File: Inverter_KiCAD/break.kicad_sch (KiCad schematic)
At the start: 13 parts, among them J8 Conn_01x02, Q9 BUK9637-100E, U21 TC1412, U22 ACPL-077L

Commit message: start schematic Nucleo board
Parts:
- C57, C58, C59, C60: footprint (none) -> Capacitor_SMD:C_0402_1005Metric_Pad0.74x0.62mm_HandSolder
- R30, R31: footprint (none) -> Resistor_SMD:R_0603_1608Metric_Pad0.98x0.95mm_HandSolder
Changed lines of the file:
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@@
       (effects (font (size 1.27 1.27)) (justify left))
     )
-    (property "Footprint" "" (at 100.33 54.61 0)
+    (property "Footprint" "Capacitor_SMD:C_0402_1005Metric_Pad0.74x0.62mm_HandSolder" (at 100.33 54.61 0)
       (effects (font (size 1.27 1.27)) hide)
     )
@@
       (effects (font (size 1.27 1.27)) (justify left))
     )
-    (property "Footprint" "" (at 53.34 54.61 0)
+    (property "Footprint" "Capacitor_SMD:C_0402_1005Metric_Pad0.74x0.62mm_HandSolder" (at 53.34 54.61 0)
       (effects (font (size 1.27 1.27)) hide)
     )
@@
       (effects (font (size 1.27 1.27)) (justify left))
     )
-    (property "Footprint" "" (at 88.9 31.75 0)
+    (property "Footprint" "Resistor_SMD:R_0603_1608Metric_Pad0.98x0.95mm_HandSolder" (at 88.9 31.75 0)
       (effects (font (size 1.27 1.27)) hide)
     )
@@
       (effects (font (size 1.27 1.27)) (justify left))
     )
-    (property "Footprint" "" (at 109.22 54.61 0)
+    (property "Footprint" "Capacitor_SMD:C_0402_1005Metric_Pad0.74x0.62mm_HandSolder" (at 109.22 54.61 0)
       (effects (font (size 1.27 1.27)) hide)
     )
@@
       (effects (font (size 1.27 1.27)))
     )
-    (property "Footprint" "" (at 36.83 49.53 0)
+    (property "Footprint" "Resistor_SMD:R_0603_1608Metric_Pad0.98x0.95mm_HandSolder" (at 36.83 49.53 0)
       (effects (font (size 1.27 1.27)) hide)
     )
@@
       (effects (font (size 1.27 1.27)) (justify left))
     )
-    (property "Footprint" "" (at 62.23 54.61 0)
-      (effects (font (size 1.27 1.27)) hide)
-    )
+    (property "Footprint" "Capacitor_SMD:C_0402_1005Metric_Pad0.74x0.62mm_HandSolder" (at 62.23 54.61 0)
+      (effects (font (size 1.27 1.27)) hide)
+    )

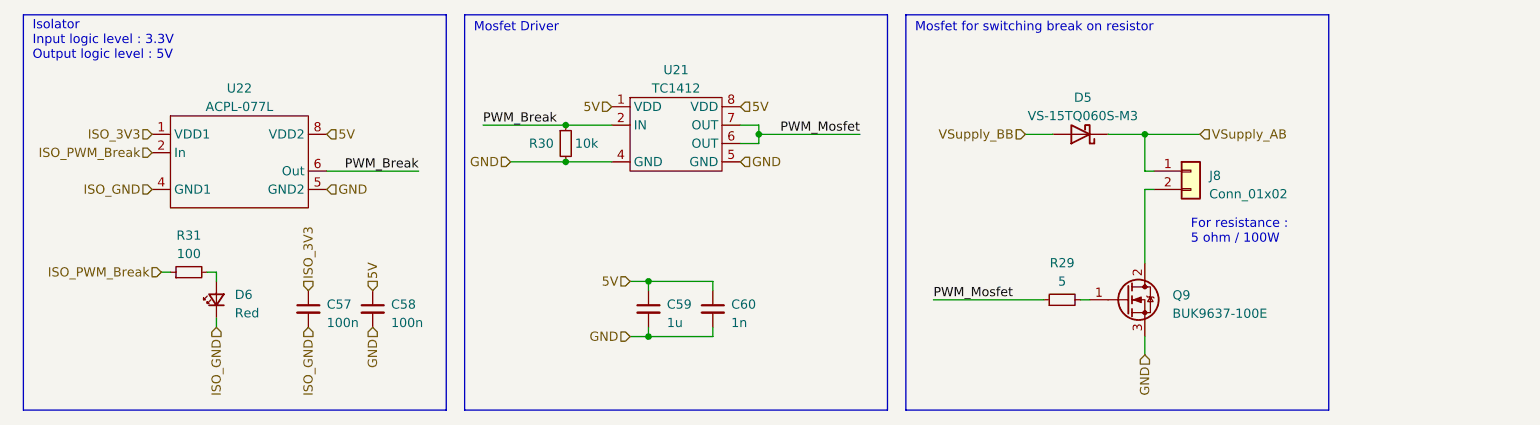
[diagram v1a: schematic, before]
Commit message: clear schematic errors
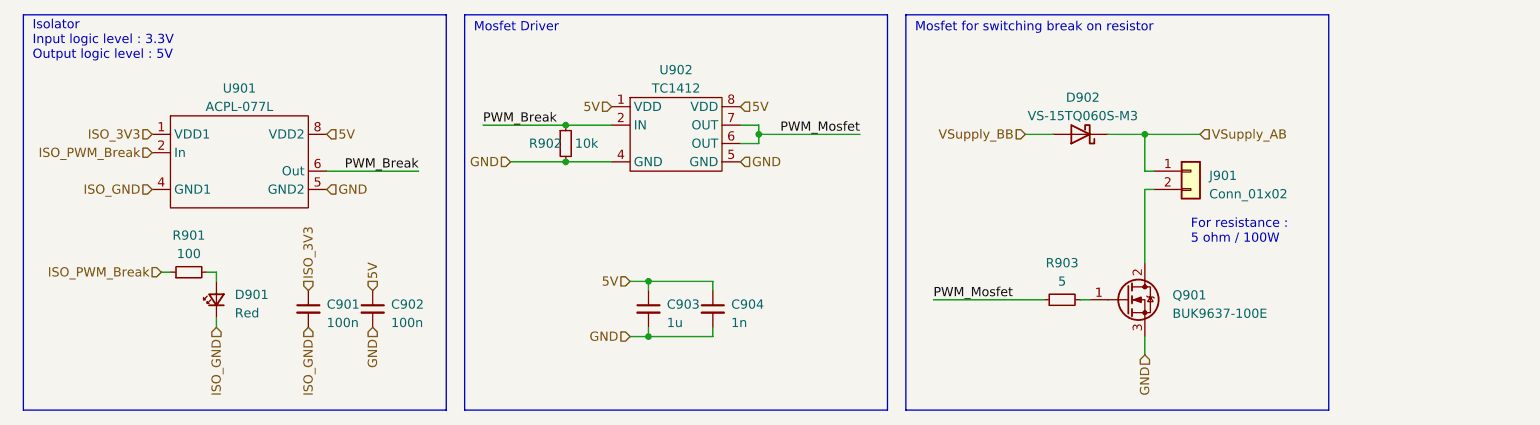
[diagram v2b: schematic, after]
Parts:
- renumbered C57 to C901, C58 to C902, C59 to C903, C60 to C904, D6 to D901, D5 to D902, J8 to J901, Q9 to Q901, R31 to R901, R30 to R902, R29 to R903, U22 to U901, U21 to U902
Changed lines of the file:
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@@
   (symbol (lib_id "Custom:TC1412") (at 104.14 30.48 0) (unit 1)
     (in_bom yes) (on_board yes) (dnp no) (fields_autoplaced)
-    (property "Reference" "U21" (at 104.14 21.59 0)
+    (property "Reference" "U902" (at 104.14 21.59 0)
       (effects (font (size 1.27 1.27)))
     )
@@
       (project "Inverter_KiCAD"
         (path "/5e6c1e3f-0815-454a-8acb-8e3e2d064875/63722f1b-78db-4d3b-ade4-7dd7cc6c956f"
-          (reference "U21") (unit 1)
+          (reference "U902") (unit 1)
         )
       )
@@
   (symbol (lib_id "Device:R_Small") (at 157.48 53.34 90) (unit 1)
     (in_bom yes) (on_board yes) (dnp no) (fields_autoplaced)
-    (property "Reference" "R29" (at 157.48 48.26 90)
+    (property "Reference" "R903" (at 157.48 48.26 90)
       (effects (font (size 1.27 1.27)))
     )
@@
       (project "Inverter_KiCAD"
         (path "/5e6c1e3f-0815-454a-8acb-8e3e2d064875/63722f1b-78db-4d3b-ade4-7dd7cc6c956f"
-          (reference "R29") (unit 1)
+          (reference "R903") (unit 1)
         )
       )
@@
   (symbol (lib_id "Device:C_Small") (at 100.33 54.61 0) (unit 1)
     (in_bom yes) (on_board yes) (dnp no) (fields_autoplaced)
-    (property "Reference" "C59" (at 102.87 53.9813 0)
+    (property "Reference" "C903" (at 102.87 53.9813 0)
       (effects (font (size 1.27 1.27)) (justify left))
     )
@@
       (project "Inverter_KiCAD"
         (path "/5e6c1e3f-0815-454a-8acb-8e3e2d064875/63722f1b-78db-4d3b-ade4-7dd7cc6c956f"
-          (reference "C59") (unit 1)
+          (reference "C903") (unit 1)
         )
       )
@@
   (symbol (lib_id "Device:C_Small") (at 53.34 54.61 0) (unit 1)
     (in_bom yes) (on_board yes) (dnp no) (fields_autoplaced)
-    (property "Reference" "C57" (at 55.88 53.9813 0)
+    (property "Reference" "C901" (at 55.88 53.9813 0)
       (effects (font (size 1.27 1.27)) (justify left))
     )
@@
       (project "Inverter_KiCAD"
         (path "/5e6c1e3f-0815-454a-8acb-8e3e2d064875/63722f1b-78db-4d3b-ade4-7dd7cc6c956f"
-          (reference "C57") (unit 1)
+          (reference "C901") (unit 1)
         )
       )
@@
   (symbol (lib_id "Device:D_Schottky") (at 160.02 30.48 180) (unit 1)
     (in_bom yes) (on_board yes) (dnp no) (fields_autoplaced)
-    (property "Reference" "D5" (at 160.3375 25.4 0)
+    (property "Reference" "D902" (at 160.3375 25.4 0)
       (effects (font (size 1.27 1.27)))
     )
@@
       (project "Inverter_KiCAD"
         (path "/5e6c1e3f-0815-454a-8acb-8e3e2d064875/63722f1b-78db-4d3b-ade4-7dd7cc6c956f"
-          (reference "D5") (unit 1)
+          (reference "D902") (unit 1)
         )
       )
@@
   (symbol (lib_id "Connector_Generic:Conn_01x02") (at 175.26 35.56 0) (unit 1)
     (in_bom yes) (on_board yes) (dnp no) (fields_autoplaced)
-    (property "Reference" "J8" (at 177.8 36.195 0)
+    (property "Reference" "J901" (at 177.8 36.195 0)
       (effects (font (size 1.27 1.27)) (justify left))
     )
@@
       (project "Inverter_KiCAD"
         (path "/5e6c1e3f-0815-454a-8acb-8e3e2d064875/63722f1b-78db-4d3b-ade4-7dd7cc6c956f"
-          (reference "J8") (unit 1)
+          (reference "J901") (unit 1)
         )
       )
@@
   (symbol (lib_id "Device:LED_Small") (at 40.64 53.34 90) (unit 1)
     (in_bom yes) (on_board yes) (dnp no) (fields_autoplaced)
-    (property "Reference" "D6" (at 43.18 52.6415 90)
+    (property "Reference" "D901" (at 43.18 52.6415 90)
       (effects (font (size 1.27 1.27)) (justify right))
     )
@@
       (project "Inverter_KiCAD"
         (path "/5e6c1e3f-0815-454a-8acb-8e3e2d064875/63722f1b-78db-4d3b-ade4-7dd7cc6c956f"
-          (reference "D6") (unit 1)
+          (reference "D901") (unit 1)
         )
       )
@@
   (symbol (lib_id "Device:R_Small") (at 88.9 31.75 0) (unit 1)
     (in_bom yes) (on_board yes) (dnp no)
-    (property "Reference" "R30" (at 83.82 31.75 0)
+    (property "Reference" "R902" (at 83.82 31.75 0)
       (effects (font (size 1.27 1.27)) (justify left))
     )
@@
       (project "Inverter_KiCAD"
         (path "/5e6c1e3f-0815-454a-8acb-8e3e2d064875/63722f1b-78db-4d3b-ade4-7dd7cc6c956f"
-          (reference "R30") (unit 1)
+          (reference "R902") (unit 1)
         )
       )
@@
   (symbol (lib_id "Custom:ACPL-077L") (at 44.45 34.29 0) (unit 1)
     (in_bom yes) (on_board yes) (dnp no) (fields_autoplaced)
-    (property "Reference" "U22" (at 43.815 24.13 0)
+    (property "Reference" "U901" (at 43.815 24.13 0)
       (effects (font (size 1.27 1.27)))
     )
@@
       (project "Inverter_KiCAD"
         (path "/5e6c1e3f-0815-454a-8acb-8e3e2d064875/63722f1b-78db-4d3b-ade4-7dd7cc6c956f"
-          (reference "U22") (unit 1)
+          (reference "U901") (unit 1)
         )
       )
@@
   (symbol (lib_id "Transistor_FET:IRFS4229") (at 166.37 53.34 0) (unit 1)
     (in_bom yes) (on_board yes) (dnp no) (fields_autoplaced)
-    (property "Reference" "Q9" (at 172.72 52.705 0)
+    (property "Reference" "Q901" (at 172.72 52.705 0)
       (effects (font (size 1.27 1.27)) (justify left))
     )
@@
       (project "Inverter_KiCAD"
         (path "/5e6c1e3f-0815-454a-8acb-8e3e2d064875/63722f1b-78db-4d3b-ade4-7dd7cc6c956f"
-          (reference "Q9") (unit 1)
+          (reference "Q901") (unit 1)
         )
       )
@@
   (symbol (lib_id "Device:C_Small") (at 109.22 54.61 0) (unit 1)
     (in_bom yes) (on_board yes) (dnp no) (fields_autoplaced)
-    (property "Reference" "C60" (at 111.76 53.9813 0)
+    (property "Reference" "C904" (at 111.76 53.9813 0)
       (effects (font (size 1.27 1.27)) (justify left))
     )
@@
       (project "Inverter_KiCAD"
         (path "/5e6c1e3f-0815-454a-8acb-8e3e2d064875/63722f1b-78db-4d3b-ade4-7dd7cc6c956f"
-          (reference "C60") (unit 1)
+          (reference "C904") (unit 1)
         )
       )
@@
   (symbol (lib_id "Device:R_Small") (at 36.83 49.53 90) (unit 1)
     (in_bom yes) (on_board yes) (dnp no) (fields_autoplaced)
-    (property "Reference" "R31" (at 36.83 44.45 90)
+    (property "Reference" "R901" (at 36.83 44.45 90)
       (effects (font (size 1.27 1.27)))
     )
@@
       (project "Inverter_KiCAD"
         (path "/5e6c1e3f-0815-454a-8acb-8e3e2d064875/63722f1b-78db-4d3b-ade4-7dd7cc6c956f"
-          (reference "R31") (unit 1)
+          (reference "R901") (unit 1)
         )
       )
@@
   (symbol (lib_id "Device:C_Small") (at 62.23 54.61 0) (unit 1)
     (in_bom yes) (on_board yes) (dnp no) (fields_autoplaced)
-    (property "Reference" "C58" (at 64.77 53.9813 0)
+    (property "Reference" "C902" (at 64.77 53.9813 0)
       (effects (font (size 1.27 1.27)) (justify left))
     )
@@
       (project "Inverter_KiCAD"
         (path "/5e6c1e3f-0815-454a-8acb-8e3e2d064875/63722f1b-78db-4d3b-ade4-7dd7cc6c956f"
-          (reference "C58") (unit 1)
-        )
-      )
+          (reference "C902") (unit 1)
+        )
+      )

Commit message: end of sch, start pcb
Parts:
- D901: footprint (none) -> LED_SMD:LED_0603_1608Metric_Pad1.05x0.95mm_HandSolder
- D902: footprint (none) -> Package_TO_SOT_SMD:TO-263-2
- J901: MFR (none) -> 691311700002
- R901, R902: footprint Resistor_SMD:R_0603_1608Metric_Pad0.98x0.95mm_HandSolder -> Resistor_SMD:R_0402_1005Metric_Pad0.72x0.64mm_HandSolder
- U902: footprint (none) -> Package_SO:SOIC-8_3.9x4.9mm_P1.27mm
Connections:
- net VSupply_AB: now also D902.2 (K); no longer D902.1 (K)
- net VSupply_BB: now also D902.3 (A); no longer D902.2 (A)
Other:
- company: (none) -> ENSEA
- title: (none) -> AAP Inverter
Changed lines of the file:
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@@
 (kicad_sch (version 20230121) (generator eeschema)
   (paper "A4")
+  (title_block
+    (title "AAP Inverter")
+    (date "2023-05-01")
+    (company "ENSEA")
+  )
   (junction (at 115.57 30.48) (diameter 0) (color 0 0 0 0)
   )
@@
       (effects (font (size 1.27 1.27)))
     )
-    (property "Footprint" "" (at 99.06 26.67 0)
+    (property "Footprint" "Package_SO:SOIC-8_3.9x4.9mm_P1.27mm" (at 99.06 26.67 0)
       (effects (font (size 1.27 1.27)) hide)
     )
@@
       (effects (font (size 1.27 1.27)))
     )
-    (property "Footprint" "" (at 160.02 30.48 0)
+    (property "Footprint" "Package_TO_SOT_SMD:TO-263-2" (at 160.02 30.48 0)
       (effects (font (size 1.27 1.27)) hide)
     )
@@
       (effects (font (size 1.27 1.27)) hide)
     )
-    (pin "1")
-    (pin "2")
+    (pin "2")
+    (pin "3")
     (instances
       (project "Inverter_KiCAD"
@@
       (effects (font (size 1.27 1.27)) hide)
     )
-    (property "Datasheet" "~" (at 175.26 35.56 0)
+    (property "Datasheet" "https://www.we-online.com/components/products/datasheet/691311700002.pdf" (at 175.26 35.56 0)
+      (effects (font (size 1.27 1.27)) hide)
+    )
+    (property "MFR" "691311700002" (at 175.26 35.56 0)
+      (effects (font (size 1.27 1.27)) hide)
+    )
+    (property "Field5" "" (at 175.26 35.56 0)
       (effects (font (size 1.27 1.27)) hide)
     )
@@
       (effects (font (size 1.27 1.27)) (justify right))
     )
-    (property "Footprint" "" (at 40.64 53.34 90)
+    (property "Footprint" "LED_SMD:LED_0603_1608Metric_Pad1.05x0.95mm_HandSolder" (at 40.64 53.34 90)
       (effects (font (size 1.27 1.27)) hide)
     )
@@
       (effects (font (size 1.27 1.27)) (justify left))
     )
-    (property "Footprint" "Resistor_SMD:R_0603_1608Metric_Pad0.98x0.95mm_HandSolder" (at 88.9 31.75 0)
+    (property "Footprint" "Resistor_SMD:R_0402_1005Metric_Pad0.72x0.64mm_HandSolder" (at 88.9 31.75 0)
       (effects (font (size 1.27 1.27)) hide)
     )
@@
       (effects (font (size 1.27 1.27)))
     )
-    (property "Footprint" "Resistor_SMD:R_0603_1608Metric_Pad0.98x0.95mm_HandSolder" (at 36.83 49.53 0)
-      (effects (font (size 1.27 1.27)) hide)
-    )
+    (property "Footprint" "Resistor_SMD:R_0402_1005Metric_Pad0.72x0.64mm_HandSolder" (at 36.83 49.53 0)
+      (effects (font (size 1.27 1.27)) hide)
+    )

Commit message: rooting done
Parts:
- J901: footprint (none) -> Custom:691311700002
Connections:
- net VSupply_AB: now also J901.2 (Pin_2); no longer J901.1 (Pin_1)
- net Break_Drain_Mosfet: now reaches Q901.2 (D)
- net Break_Drain_Mosfet: now also J901.1 (Pin_1); no longer J901.2 (Pin_2)
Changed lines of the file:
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@@
+    (effects (font (size 1.27 1.27)) (justify right bottom))
+  )
+  (label "Break_Drain_Mosfet" (at 168.91 44.45 180) (fields_autoplaced)
     (effects (font (size 1.27 1.27)) (justify right bottom))
   )
@@
     )
   )
-  (symbol (lib_id "Connector_Generic:Conn_01x02") (at 175.26 35.56 0) (unit 1)
-    (in_bom yes) (on_board yes) (dnp no) (fields_autoplaced)
-    (property "Reference" "J901" (at 177.8 36.195 0)
-      (effects (font (size 1.27 1.27)) (justify left))
-    )
-    (property "Value" "Conn_01x02" (at 177.8 38.735 0)
-      (effects (font (size 1.27 1.27)) (justify left))
-    )
-    (property "Footprint" "" (at 175.26 35.56 0)
-      (effects (font (size 1.27 1.27)) hide)
-    )
-    (property "Datasheet" "https://www.we-online.com/components/products/datasheet/691311700002.pdf" (at 175.26 35.56 0)
-      (effects (font (size 1.27 1.27)) hide)
-    )
-    (property "MFR" "691311700002" (at 175.26 35.56 0)
-      (effects (font (size 1.27 1.27)) hide)
-    )
-    (property "Field5" "" (at 175.26 35.56 0)
-      (effects (font (size 1.27 1.27)) hide)
-    )
+  (symbol (lib_id "Connector_Generic:Conn_01x02") (at 175.26 38.1 0) (mirror x) (unit 1)
+    (in_bom yes) (on_board yes) (dnp no)
+    (property "Reference" "J901" (at 175.26 30.48 0)
+      (effects (font (size 1.27 1.27)))
+    )
+    (property "Value" "Conn_01x02" (at 175.26 33.02 0)
+      (effects (font (size 1.27 1.27)))
+    )
+    (property "Footprint" "Custom:691311700002" (at 175.26 38.1 0)
+      (effects (font (size 1.27 1.27)) hide)
+    )
+    (property "Datasheet" "https://www.we-online.com/components/products/datasheet/691311700002.pdf" (at 175.26 38.1 0)
+      (effects (font (size 1.27 1.27)) hide)
+    )
+    (property "MFR" "691311700002" (at 175.26 38.1 0)
+      (effects (font (size 1.27 1.27)) hide)
+    )
+    (property "Field5" "" (at 175.26 38.1 0)
+      (effects (font (size 1.27 1.27)) hide)
+    )

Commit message: apply changes
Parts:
- added D1: VS-15TQ060S-M3, Package_TO_SOT_SMD:TO-263-2, symbol Device:D_Schottky
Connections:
- net Break_Drain_Mosfet: now also D1.3 (A)
- net VSupply_AB: now also D1.2 (K)
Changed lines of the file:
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@@
   (junction (at 115.57 30.48) (diameter 0) (color 0 0 0 0)
   )
+  (junction (at 168.91 33.02) (diameter 0) (color 0 0 0 0)
+  )
+  (junction (at 168.91 40.64) (diameter 0) (color 0 0 0 0)
+  )
   (junction (at 88.9 29.21) (diameter 0) (color 0 0 0 0)
   )
@@
     (stroke (width 0) (type default))
   )
-  (wire (pts (xy 168.91 38.1) (xy 168.91 48.26))
+  (wire (pts (xy 168.91 38.1) (xy 168.91 40.64))
     (stroke (width 0) (type default))
   )
@@
     (stroke (width 0) (type default))
   )
+  (wire (pts (xy 165.1 33.02) (xy 168.91 33.02))
+    (stroke (width 0) (type default))
+  )
   (wire (pts (xy 115.57 30.48) (xy 115.57 31.75))
     (stroke (width 0) (type default))
   )
+  (wire (pts (xy 168.91 40.64) (xy 168.91 48.26))
+    (stroke (width 0) (type default))
+  )
   (wire (pts (xy 109.22 58.42) (xy 109.22 57.15))
     (stroke (width 0) (type default))
@@
     (stroke (width 0) (type default))
   )
+  (wire (pts (xy 168.91 33.02) (xy 168.91 35.56))
+    (stroke (width 0) (type default))
+  )
   (wire (pts (xy 40.64 55.88) (xy 40.64 57.15))
     (stroke (width 0) (type default))
@@
     (stroke (width 0) (type default))
   )
-  (wire (pts (xy 168.91 30.48) (xy 168.91 35.56))
+  (wire (pts (xy 168.91 30.48) (xy 168.91 33.02))
     (stroke (width 0) (type default))
   )
@@
   )
   (wire (pts (xy 88.9 29.21) (xy 95.25 29.21))
+    (stroke (width 0) (type default))
+  )
+  (wire (pts (xy 165.1 40.64) (xy 168.91 40.64))
     (stroke (width 0) (type default))
   )
@@
         )
       )
+    )
+  )
+  (symbol (lib_id "Device:D_Schottky") (at 165.1 36.83 270) (unit 1)
+    (in_bom yes) (on_board yes) (dnp no)
+    (property "Reference" "D1" (at 160.02 35.56 90)
+      (effects (font (size 1.27 1.27)) (justify left))
+    )
+    (property "Value" "VS-15TQ060S-M3" (at 144.78 38.1 90)
+      (effects (font (size 1.27 1.27)) (justify left))
+    )
+    (property "Footprint" "Package_TO_SOT_SMD:TO-263-2" (at 165.1 36.83 0)
+      (effects (font (size 1.27 1.27)) hide)
+    )
+    (property "Datasheet" "~" (at 165.1 36.83 0)
+      (effects (font (size 1.27 1.27)) hide)
+    )
+    (pin "2")
+    (pin "3")
+    (instances
+      (project "Inverter_KiCAD"
+        (path "/5e6c1e3f-0815-454a-8acb-8e3e2d064875/63722f1b-78db-4d3b-ade4-7dd7cc6c956f"
+          (reference "D1") (unit 1)
+        )
+      )

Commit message: Update KiCAD
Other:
- note added: "nouvelle ref : 691311500102"
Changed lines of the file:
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@@
     (effects (font (size 1.27 1.27)) (justify left bottom))
+  )
+  (text "nouvelle ref : \n691311500102" (at 175.26 26.67 0)
+    (effects (font (size 3.4 3.4) (thickness 0.68) bold) (justify left bottom))
   )
   (text "For resistance :\n5 ohm / 100W" (at 175.26 45.72 0)
